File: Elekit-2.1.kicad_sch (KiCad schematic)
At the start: 115 parts, among them J101 Conn_01x03_Male, J102 Conn_01x03_Male, J103 Screw_Terminal_01x02, J104 Conn_01x03_Male, J105 Conn_01x01_Pin, J106 Conn_01x01_Pin, J107 Conn_01x01_Pin, J108 Conn_01x01_Pin, J111 Conn_01x01_Pin, J112 Conn_01x01_Pin, J113 Conn_01x01_Pin, J117 Conn_01x01_Pin, J118 Conn_01x01_Pin, J119 Conn_01x01_Pin, J120 Conn_01x01_Pin, J121 Conn_01x01_Pin, J122 Conn_01x01_Pin, J2 Screw_Terminal_01x02, J3 Screw_Terminal_01x02, J4 Screw_Terminal_01x02, J5 Conn_01x03_Male, J6 Conn_01x06_Male, J7 Conn_01x04, J9 Conn_01x03_Male, Q1 2N7002, Q101 2N7002, Q3 2N7002, U1 MINI_5PTP, U10 TS-1187A-B-A-B, U101 DRV8876PWPR, U102 DRV8876PWPR, U103 LSM303AGRTR, U104 DRV8876PWPR, U106 TS-1187A-B-A-B, U107 R-78E5.0-0.5, U5 SRV05-4-P-T7, U7 ME6211C33M5G-N, U8 TS-1187A-B-A-B, U9 ESP32-C3-WROOM-02-N4(4MB)

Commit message: add jst ph connector for lidar
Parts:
- removed J7: Conn_01x04, Connector_PinSocket_2.54mm:PinSocket_1x04_P2.54mm_Vertical, symbol Connector_Generic:Conn_01x04
- added J109: Conn_01x04_Socket, Connector_JST:JST_PH_S4B-PH-K_1x04_P2.00mm_Horizontal, symbol Connector:Conn_01x04_Socket
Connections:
- net +5V: now also J109.4 (Pin_4)
- net GND: now also J109.3 (Pin_3)
- net RX: now also J109.1 (Pin_1)
- net TX: now also J109.2 (Pin_2)
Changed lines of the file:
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@@
     (effects (font (size 1.27 1.27)) (justify left))
   )
+  (hierarchical_label "RX" (shape input) (at 270.51 124.46 270) (fields_autoplaced)
+    (effects (font (size 1.27 1.27)) (justify right))
+  )
   (hierarchical_label "B2_C" (shape input) (at 124.46 267.97 0) (fields_autoplaced)
     (effects (font (size 1.27 1.27)) (justify left))
@@
     (effects (font (size 1.27 1.27)) (justify right))
   )
+  (hierarchical_label "TX" (shape input) (at 273.05 124.46 270) (fields_autoplaced)
+    (effects (font (size 1.27 1.27)) (justify right))
+  )
   (hierarchical_label "A2_C" (shape input) (at 124.46 273.05 0) (fields_autoplaced)
     (effects (font (size 1.27 1.27)) (justify left))
@@
     )
   )
+  (symbol (lib_id "power:GND") (at 275.59 124.46 0) (unit 1)
+    (in_bom yes) (on_board yes) (dnp no)
+    (property "Reference" "#PWR0168" (at 275.59 130.81 0)
+      (effects (font (size 1.27 1.27)) hide)
+    )
+    (property "Value" "GND" (at 275.59 129.54 90)
+      (effects (font (size 1.27 1.27)))
+    )
+    (property "Footprint" "" (at 275.59 124.46 0)
+      (effects (font (size 1.27 1.27)) hide)
+    )
+    (property "Datasheet" "" (at 275.59 124.46 0)
+      (effects (font (size 1.27 1.27)) hide)
+    )
+    (pin "1")
+    (instances
+      (project "Elekit-2.1"
+        (path "/dbb28e6b-f577-4188-b79a-6034750f3ec5"
+          (reference "#PWR0168") (unit 1)
+        )
+      )
+    )
+  )
   (symbol (lib_id "power:GND") (at 372.11 182.88 0) (mirror y) (unit 1)
     (in_bom yes) (on_board yes) (dnp no)
@@
     )
   )
-  (symbol (lib_id "power:+3.3V") (at 158.75 248.92 90) (mirror x) (unit 1)
-    (in_bom yes) (on_board yes) (dnp no)
-    (property "Reference" "#PWR0109" (at 162.56 248.92 0)
-      (effects (font (size 1.27 1.27)) hide)
-    )
-    (property "Value" "+3.3V" (at 154.94 248.92 0)
-      (effects (font (size 1.27 1.27)))
-    )
-    (property "Footprint" "" (at 158.75 248.92 0)
-      (effects (font (size 1.27 1.27)) hide)
-    )
-    (property "Datasheet" "" (at 158.75 248.92 0)
-      (effects (font (size 1.27 1.27)) hide)
-    )
-    (pin "1")
-    (instances
-      (project "Elekit-2.1"
-        (path "/dbb28e6b-f577-4188-b79a-6034750f3ec5"
-          (reference "#PWR0109") (unit 1)
-        )
-      )
-    )
-  )
   (symbol (lib_id "Jumper:SolderJumper_2_Open") (at 74.93 252.73 180) (unit 1)
     (in_bom no) (on_board yes) (dnp no)
@@
     )
   )
+  (symbol (lib_id "Connector:Conn_01x04_Socket") (at 273.05 119.38 90) (unit 1)
+    (in_bom yes) (on_board yes) (dnp no) (fields_autoplaced)
+    (property "Reference" "J109" (at 274.32 114.3 90)
+      (effects (font (size 1.27 1.27)))
+    )
+    (property "Value" "Conn_01x04_Socket" (at 274.32 116.84 90)
+      (effects (font (size 1.27 1.27)))
+    )
+    (property "Footprint" "Connector_JST:JST_PH_S4B-PH-K_1x04_P2.00mm_Horizontal" (at 273.05 119.38 0)
+      (effects (font (size 1.27 1.27)) hide)
+    )
+    (property "Datasheet" "~" (at 273.05 119.38 0)
+      (effects (font (size 1.27 1.27)) hide)
+    )
+    (pin "1")
+    (pin "2")
+    (pin "3")
+    (pin "4")
+    (instances
+      (project "Elekit-2.1"
+        (path "/dbb28e6b-f577-4188-b79a-6034750f3ec5"
+          (reference "J109") (unit 1)
+        )
+      )
+    )
+  )
   (symbol (lib_id "Device:C_Small") (at 107.95 139.7 0) (mirror x) (unit 1)
     (in_bom yes) (on_board yes) (dnp no)
@@
     )
   )
-  (symbol (lib_id "power:GND") (at 158.75 241.3 270) (unit 1)
-    (in_bom yes) (on_board yes) (dnp no)
-    (property "Reference" "#PWR0114" (at 152.4 241.3 0)
-      (effects (font (size 1.27 1.27)) hide)
-    )
-    (property "Value" "GND" (at 153.67 241.3 90)
-      (effects (font (size 1.27 1.27)))
-    )
-    (property "Footprint" "" (at 158.75 241.3 0)
-      (effects (font (size 1.27 1.27)) hide)
-    )
-    (property "Datasheet" "" (at 158.75 241.3 0)
-      (effects (font (size 1.27 1.27)) hide)
-    )
-    (pin "1")
-    (instances
-      (project "Elekit-2.1"
-        (path "/dbb28e6b-f577-4188-b79a-6034750f3ec5"
-          (reference "#PWR0114") (unit 1)
-        )
-      )
-    )
-  )
   (symbol (lib_id "0_JLCPCB_Symbols:ME6211C33M5G-N") (at 394.97 257.81 0) (unit 1)
     (in_bom yes) (on_board yes) (dnp no) (fields_autoplaced)
@@
     )
   )
+  (symbol (lib_id "power:+5V") (at 278.13 124.46 180) (unit 1)
+    (in_bom yes) (on_board yes) (dnp no) (fields_autoplaced)
+    (property "Reference" "#PWR0167" (at 278.13 120.65 0)
+      (effects (font (size 1.27 1.27)) hide)
+    )
+    (property "Value" "+5V" (at 278.13 129.54 0)
+      (effects (font (size 1.27 1.27)))
+    )
+    (property "Footprint" "" (at 278.13 124.46 0)
+      (effects (font (size 1.27 1.27)) hide)
+    )
+    (property "Datasheet" "" (at 278.13 124.46 0)
+      (effects (font (size 1.27 1.27)) hide)
+    )
+    (pin "1")
+    (instances
+      (project "Elekit-2.1"
+        (path "/dbb28e6b-f577-4188-b79a-6034750f3ec5"
+          (reference "#PWR0167") (unit 1)
+        )
+      )
+    )
+  )
   (symbol (lib_id "Device:C_Small") (at 245.11 270.51 0) (mirror x) (unit 1)
     (in_bom yes) (on_board yes) (dnp no)
@@
         )
       )
-    )
-  )
-  (symbol (lib_id "Connector_Generic:Conn_01x04") (at 163.83 243.84 0) (unit 1)
-    (in_bom yes) (on_board yes) (dnp no) (fields_autoplaced)
-    (property "Reference" "J7" (at 166.37 243.8399 0)
-      (effects (font (size 1.27 1.27)) (justify left))
-    )
-    (property "Value" "Conn_01x04" (at 166.37 246.3799 0)
-      (effects (font (size 1.27 1.27)) (justify left))
-    )
-    (property "Footprint" "Connector_PinSocket_2.54mm:PinSocket_1x04_P2.54mm_Vertical" (at 163.83 243.84 0)
-      (effects (font (size 1.27 1.27)) hide)
-    )
-    (property "Datasheet" "~" (at 163.83 243.84 0)
-      (effects (font (size 1.27 1.27)) hide)
-    )
-    (pin "1")
-    (pin "2")
-    (pin "3")
-    (pin "4")
-    (instances
-      (project "Elekit-2.1"
-        (path "/dbb28e6b-f577-4188-b79a-6034750f3ec5"
-          (reference "J7") (unit 1)
-        )
-      )

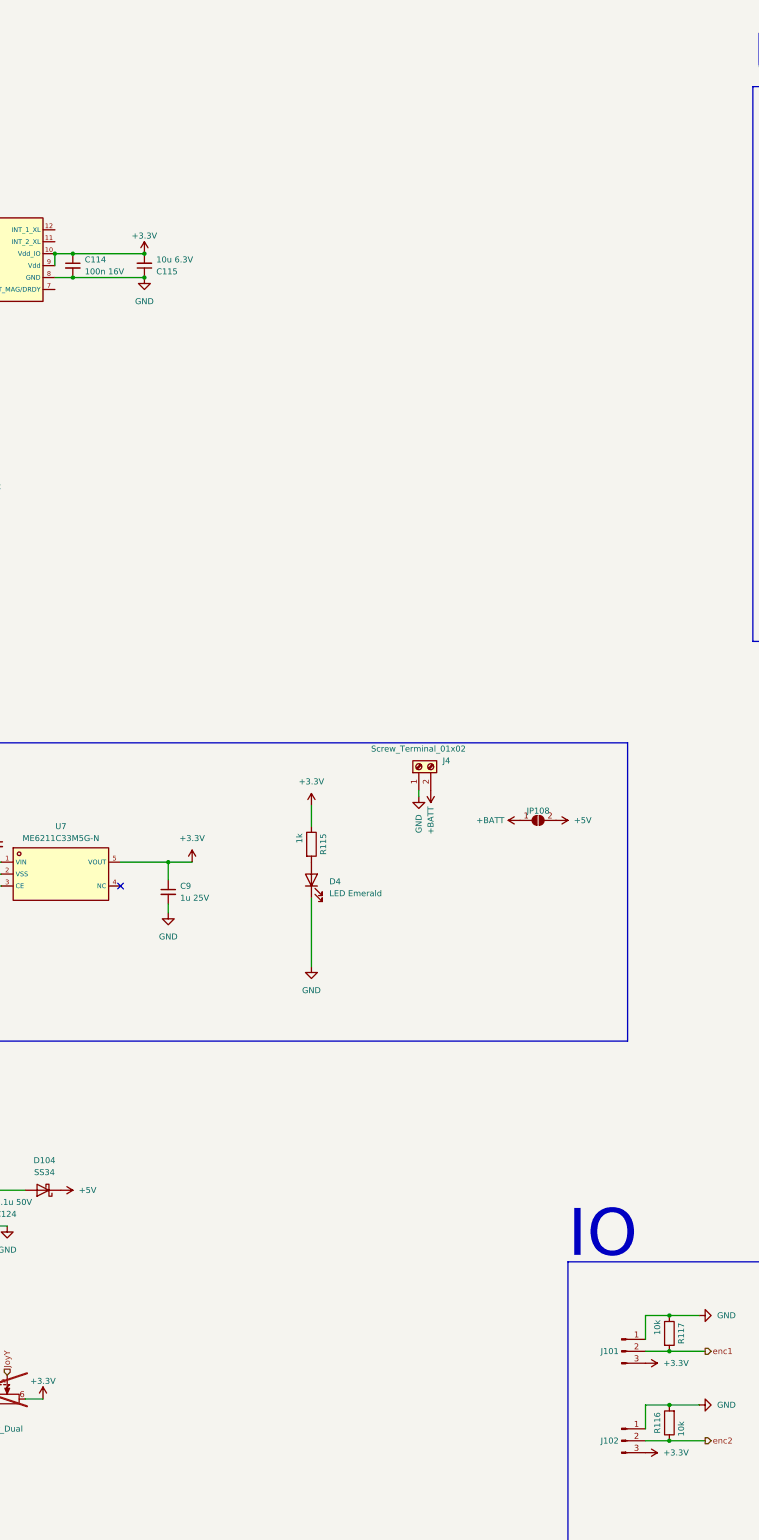
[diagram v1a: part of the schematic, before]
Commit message: add bno085
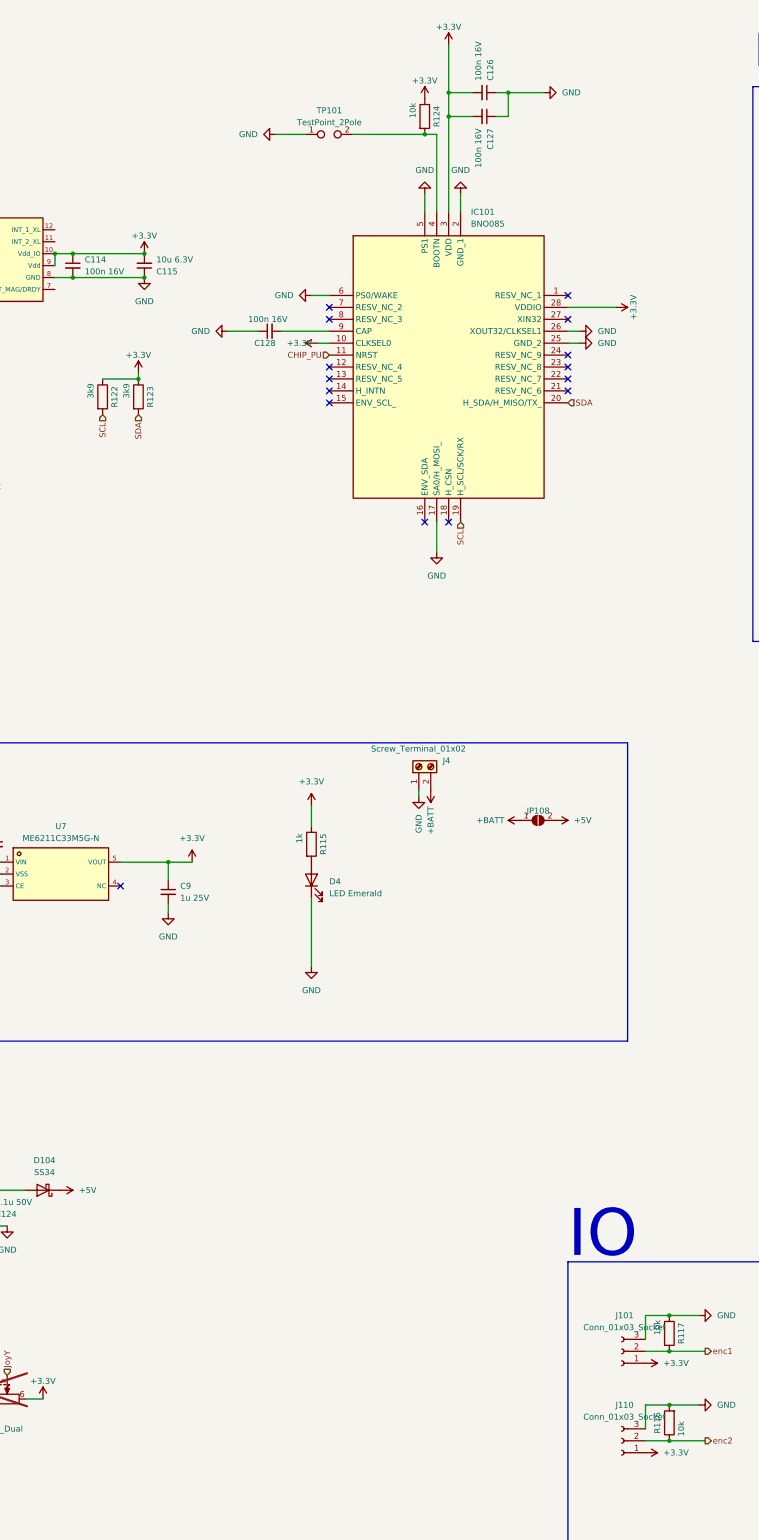
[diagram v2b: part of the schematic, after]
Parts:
- removed J101, J102: Conn_01x03_Male, Connector_PinHeader_2.54mm:PinHeader_1x03_P2.54mm_Vertical, symbol Connector:Conn_01x03_Male
- added C126, C127, C128: 100n 16V, Capacitor_SMD:C_0402_1005Metric, symbol Device:C_Small
- added IC101: BNO085, BNO085, symbol BNO085:BNO085
- added J101, J110: Conn_01x03_Socket, SnapEDA Library:TE_292173-3, symbol Connector:Conn_01x03_Socket
- added R122, R123: 3k9, Resistor_SMD:R_0603_1608Metric, symbol Device:R
- added R124: 10k, Resistor_SMD:R_0402_1005Metric, symbol Device:R
- added TP101: TestPoint_2Pole, TestPoint:TestPoint_2Pads_Pitch2.54mm_Drill0.8mm, symbol Connector:TestPoint_2Pole
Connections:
- net +3.3V: now also C126.2, C127.2, IC101.10 (CLKSEL0), IC101.28 (VDDIO), IC101.3 (VDD), J101.1 (Pin_1), J110.1 (Pin_1), R122.1, R123.1, R124.1
- net CHIP_PU: now also IC101.11 (NRST)
- net GND: now also C126.1, C127.1, C128.1, IC101.17 (SA0/H_MOSI_), IC101.2 (GND_1), IC101.25 (GND_2), IC101.26 (XOUT32/CLKSEL1), IC101.5 (PS1), IC101.6 (PS0/WAKE), J101.3 (Pin_3), J110.3 (Pin_3), TP101.1
- net GPIO5: now also J101.2 (Pin_2)
- net GPIO6: now also J110.2 (Pin_2)
- net SCL: now also IC101.19 (H_SCL/SCK/RX), R122.2
- net SDA: now also IC101.20 (H_SDA/H_MISO/TX_), R123.2
- new net: IC101.4 (BOOTN), R124.2, TP101.2
- new net: C128.2, IC101.9 (CAP)
- no-connect marks 4 -> 18
